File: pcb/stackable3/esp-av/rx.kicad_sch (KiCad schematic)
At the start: 25 parts, among them J2 PJ-327U, J3 PJ-327U, J4 PJ-327U, J5 PJ-327U, U10 SN74LVC1T45Z6, U4 NC7WZ14P6X, U5 NC7WZ14P6X, U6 SN74LVC1G157DC, U7 SN74LVC1G157DC, U8 SN74LVC1G157DC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

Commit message: Rename mode LEDs GND net on stackable3/esp-av
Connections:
- net DEBUG_LED_GND renamed MODE_LED_GND
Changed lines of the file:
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@@
 		)
 	)
-	(global_label "DEBUG_LED_GND"
+	(global_label "MODE_LED_GND"
 		(shape output)
 		(at 57.15 115.57 0)
@@
 		)
 	)
-	(global_label "DEBUG_LED_GND"
+	(global_label "MODE_LED_GND"
 		(shape output)
 		(at 57.15 151.13 0)
@@
 		)
 	)
-	(global_label "DEBUG_LED_GND"
+	(global_label "MODE_LED_GND"
 		(shape output)
 		(at 57.15 80.01 0)
@@
 		)
 	)
-	(global_label "DEBUG_LED_GND"
+	(global_label "MODE_LED_GND"
 		(shape output)
 		(at 57.15 44.45 0)

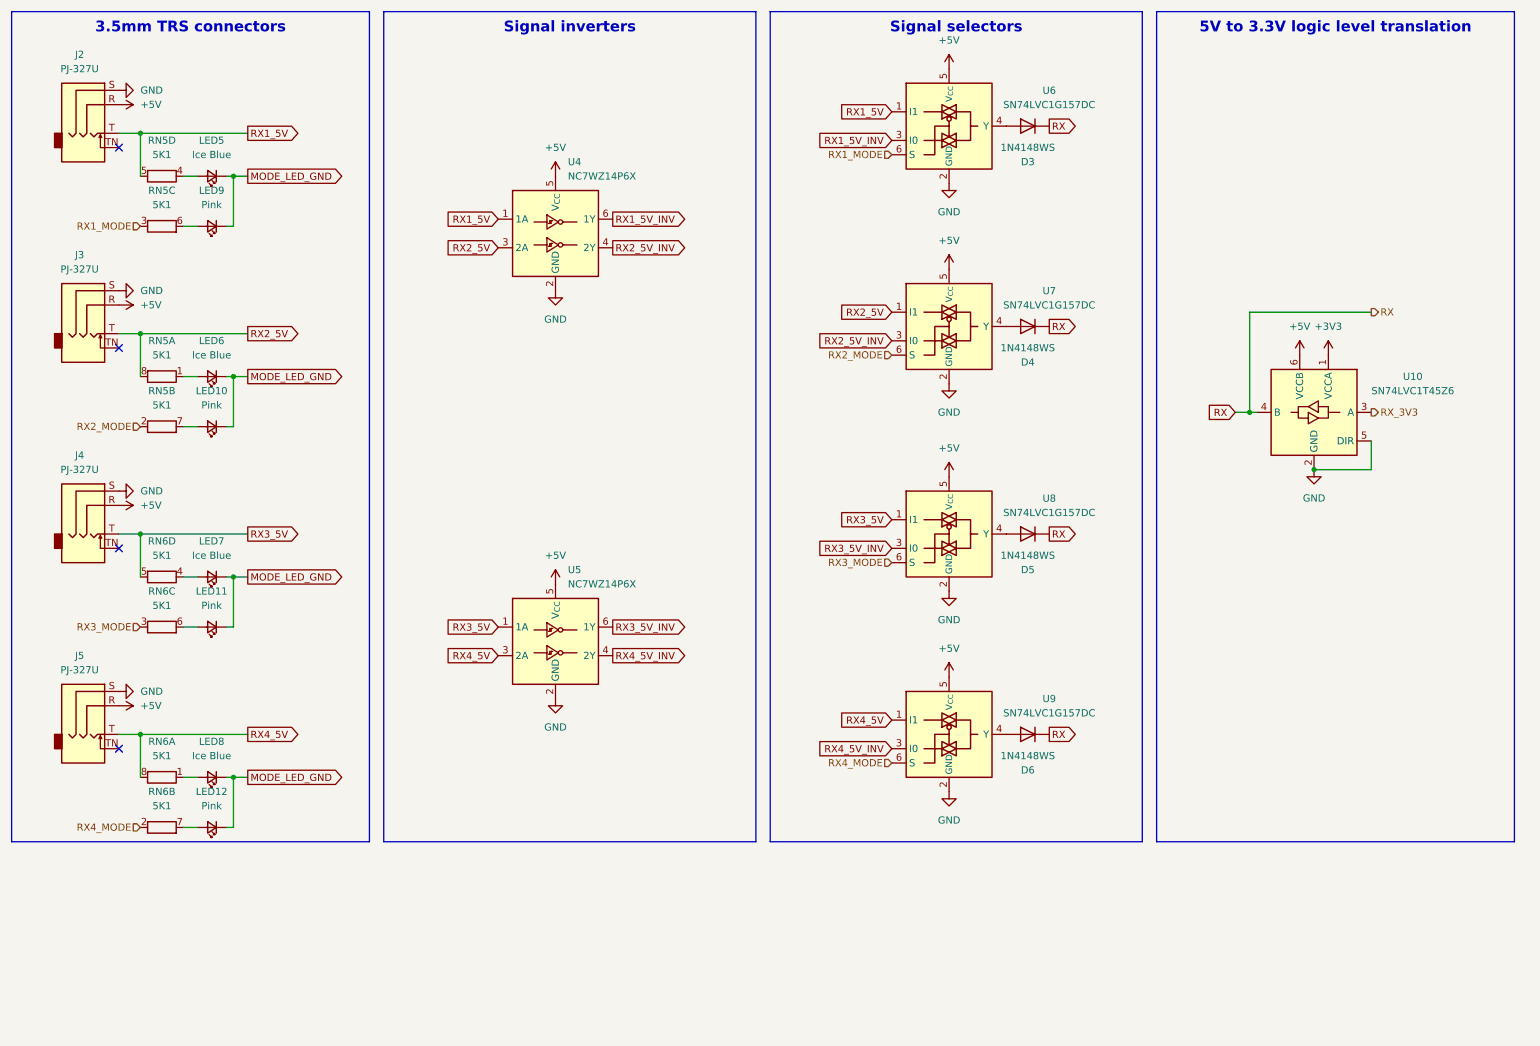
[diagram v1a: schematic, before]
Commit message: Update stackable3/esp-av to v2
Feature changes:
- Add 38kHz RX signal modulation
- Add onboard infrared receiver module (IRM)
- Add JST SH connector for 595 daisy chain outputs
- Add transmit pin socket connector tied to TX1
- Remove neopixel daisy-chain output connectors
- Move indicator LEDs toggle to a 595 output
- Swap RX multiplexer inputs so low select input is non-inverted signal
- Invert repeater enable logic to enable when low
- Add two more mounting holes to PCB

Circuit changes:
- Add power rail short protection on RX connectors
- Add reset IC for 595 start-up state control
- Connect indicator LED MOSFET gate pull-down resistors to ground
- Tie status LED to GND
- Add RX and RX mode pulldown resistors, TX 5V N-channel MOSFET drivers

Component changes:
- Use GT0104SC for logic level translation
- Use 1N5819WT for Schottky diodes
- Use SP2006KT5 P-channel MOSFET for repeater enable
- Use smaller tactile push button for GPIO9/Boot
- Use dual P-channel MOSFETs for TX and TX-5V switches
- Replace aluminum electrolytic capacitors with polymer aluminum
- Replace ME6211C33M5 LDO regulator with DS8242-33SS3
- Change RX/TX indicator LEDs color from blue to green
- Reduce solder paste amount on 0603 SMD LED footprints
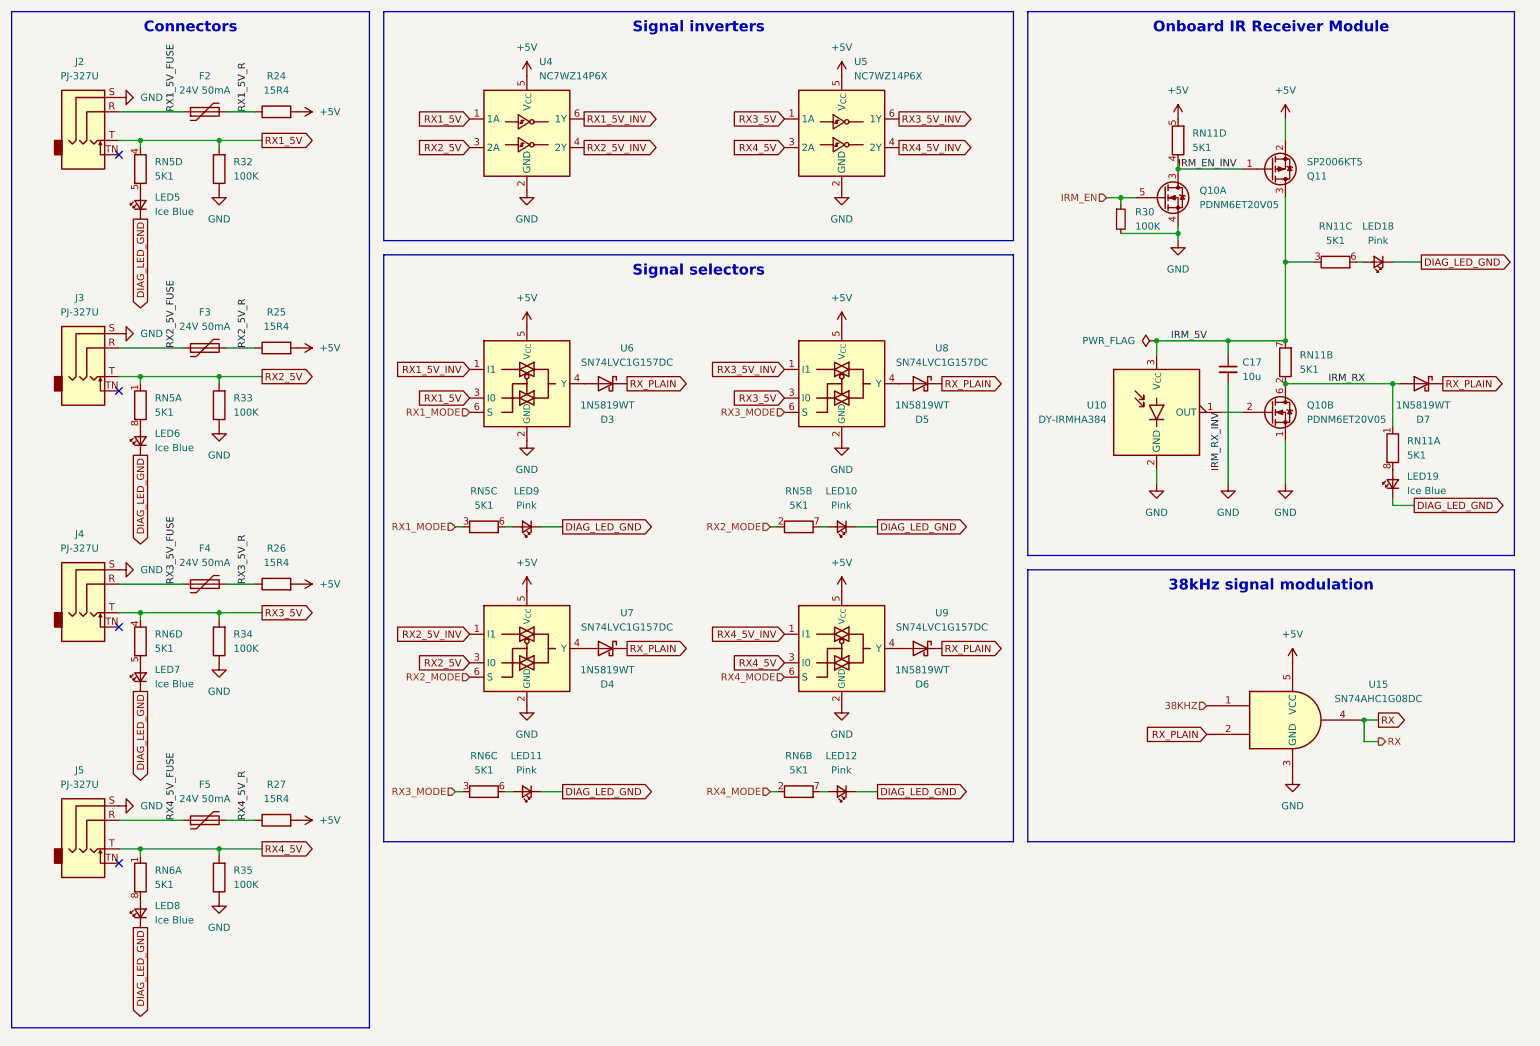
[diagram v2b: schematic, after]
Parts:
- removed D3, D4, D5, D6: 1N4148WS, package:D_SOD-323, symbol Diode:1N4148WS
- removed U10: SN74LVC1T45Z6, Package_TO_SOT_SMD:SOT-563, symbol ic:SN74LVC1T45Z6
- added C17: 10u, discrete:C_0603_1608Metric, symbol Device:C_Small
- added D3, D4, D5, D6, D7: 1N5819WT, package:D_SOD-523, symbol discrete:1N5819WT
- added F2, F3, F4, F5: 24V 50mA, Fuse:Fuse_0603_1608Metric, symbol Device:Polyfuse
- added LED18: Pink, discrete:LED_0603_1608Metric, symbol Device:LED_Small
- added LED19: Ice Blue, discrete:LED_0603_1608Metric, symbol Device:LED_Small
- added Q10: PDNM6ET20V05, Package_TO_SOT_SMD:SOT-563, symbol discrete:PDNM6ET20V05
- added Q11: SP2006KT5, package:SOT-523, symbol discrete:SP2006KT5
- added R24, R25, R26, R27: 15R4, Resistor_SMD:R_1206_3216Metric, symbol Device:R
- added R30: 100K, Resistor_SMD:R_0603_1608Metric, symbol Device:R_Small
- added R32, R33, R34, R35: 100K, Resistor_SMD:R_0603_1608Metric, symbol Device:R
- added RN11: 5K1, discrete:R_Array_Convex_4x0603, symbol Device:R_Pack04_Split
- added U10: DY-IRMHA384, package:IRM_5.0mmx4.2mm_P1.27mm_Horizontal, symbol discrete:DY-IRMHA384
- added U15: SN74AHC1G08DC, Package_TO_SOT_SMD:SOT-353_SC-70-5, symbol ic:SN74AHC1G08DC
- LED5, LED6, LED7, LED8: LCSC Part (none) -> C7496823
- RN5, RN6: footprint discrete:R_Array_Convex_4x0603_HandSolder -> discrete:R_Array_Convex_4x0603
- U4, U5, U6, U7, U8, U9: footprint package:SOT-363_SC-70-6_HandSolder -> Package_TO_SOT_SMD:SOT-363_SC-70-6
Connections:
- net +5V: now also Q11.2 (S), R24.2, R25.2, R26.2, R27.2, RN11.5 (R4.2), U15.5 (VCC); no longer J2.R, J3.R, J4.R, J5.R
- net GND: now also C17.2, Q10.1 (S), Q10.4 (S), R30.2, R32.1, R33.1, R34.1, R35.1, U10.2 (GND), U15.3 (GND)
- net RX: now also U15.4
- net RX1_5V: now also RN5.4 (R4.1), U6.3 (I0), R32.2; no longer RN5.5 (R4.2), U6.1 (I1)
- net RX1_5V_INV: now also U6.1 (I1); no longer U6.3 (I0)
- net RX2_5V: now also RN5.1 (R1.1), U7.3 (I0), R33.2; no longer RN5.8 (R1.2), U7.1 (I1)
- net RX2_5V_INV: now also U7.1 (I1); no longer U7.3 (I0)
- net RX3_5V: now also RN6.4 (R4.1), U8.3 (I0), R34.2; no longer RN6.5 (R4.2), U8.1 (I1)
- net RX3_5V_INV: now also U8.1 (I1); no longer U8.3 (I0)
- net RX4_5V: now also RN6.1 (R1.1), U9.3 (I0), R35.2; no longer RN6.8 (R1.2), U9.1 (I1)
- net RX4_5V_INV: now also U9.1 (I1); no longer U9.3 (I0)
- net at LED6.2 (A): now also RN5.8 (R1.2); no longer RN5.1 (R1.1)
- net at LED8.2 (A): now also RN6.8 (R1.2); no longer RN6.1 (R1.1)
- net at LED7.2 (A): now also RN6.5 (R4.2); no longer RN6.4 (R4.1)
- net at U8.4 (Y): now also D5.2 (A)
- net at U6.4 (Y): now also D3.2 (A)
- net at U9.4 (Y): now also D6.2 (A)
- net at LED5.2 (A): now also RN5.5 (R4.2); no longer RN5.4 (R4.1)
- net at U7.4 (Y): now also D4.2 (A)
- net MODE_LED_GND renamed DIAG_LED_GND
- net DIAG_LED_GND: now also LED18.1 (K), LED19.1 (K)
- new net: LED18.2 (A), RN11.6 (R3.2)
- new net: LED19.2 (A), RN11.8 (R1.2)
- new net 38KHZ: U15.1
- new net IRM_5V: C17.1, Q11.3 (D), RN11.3 (R3.1), RN11.7 (R2.2), U10.3 (V_{CC})
- new net IRM_EN: Q10.5 (G), R30.1
- new net IRM_EN_INV: Q10.3 (D), Q11.1 (G), RN11.4 (R4.1)
- new net IRM_RX: D7.2 (A), Q10.6 (D), RN11.1 (R1.1), RN11.2 (R2.1)
- new net IRM_RX_INV: Q10.2 (G), U10.1 (OUT)
- new net RX1_5V_FUSE: F2.1, J2.R
- new net RX1_5V_R: F2.2, R24.1
- new net RX2_5V_FUSE: F3.1, J3.R
- new net RX2_5V_R: F3.2, R25.1
- new net RX3_5V_FUSE: F4.1, J4.R
- new net RX3_5V_R: F4.2, R26.1
- new net RX4_5V_FUSE: F5.1, J5.R
- new net RX4_5V_R: F5.2, R27.1
- new net RX_PLAIN: D3.1 (K), D4.1 (K), D5.1 (K), D6.1 (K), D7.1 (K), U15.2
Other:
- moved on the sheet: J2, J3, J4, J5, LED10, LED11, LED12, LED5, LED6, LED7, LED8, LED9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
